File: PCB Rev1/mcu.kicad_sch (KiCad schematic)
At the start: 6 parts, among them SW3 RESET, SW4 BOOT, U7 ESP32-S3-MINI-1U-N8

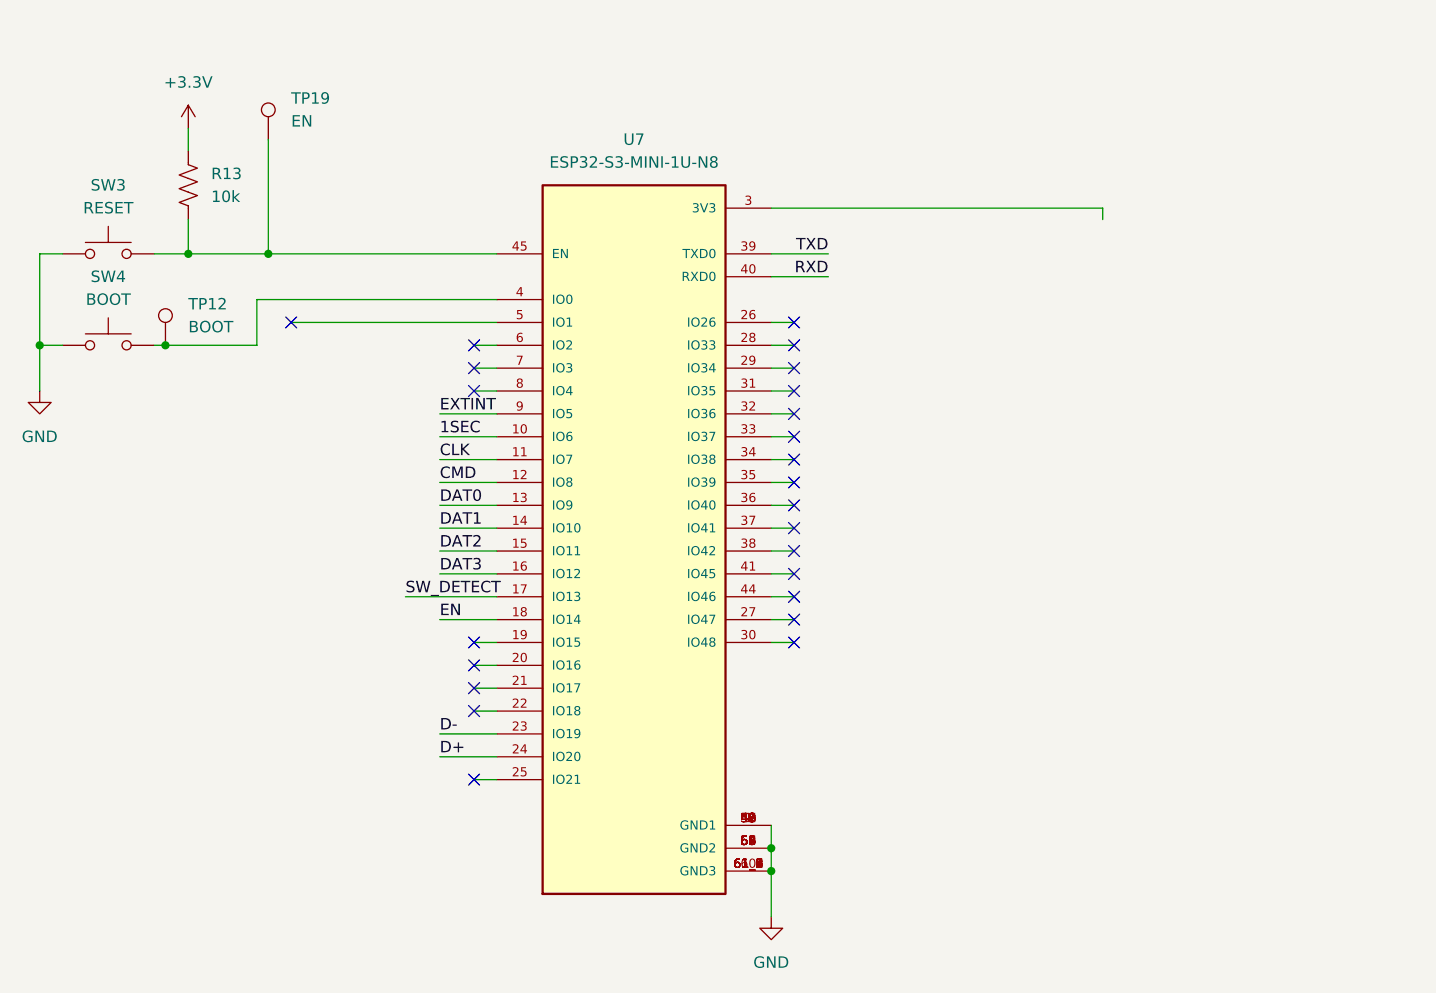
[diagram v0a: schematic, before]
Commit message: rev 2 schematic with minor changes, final send out before layout
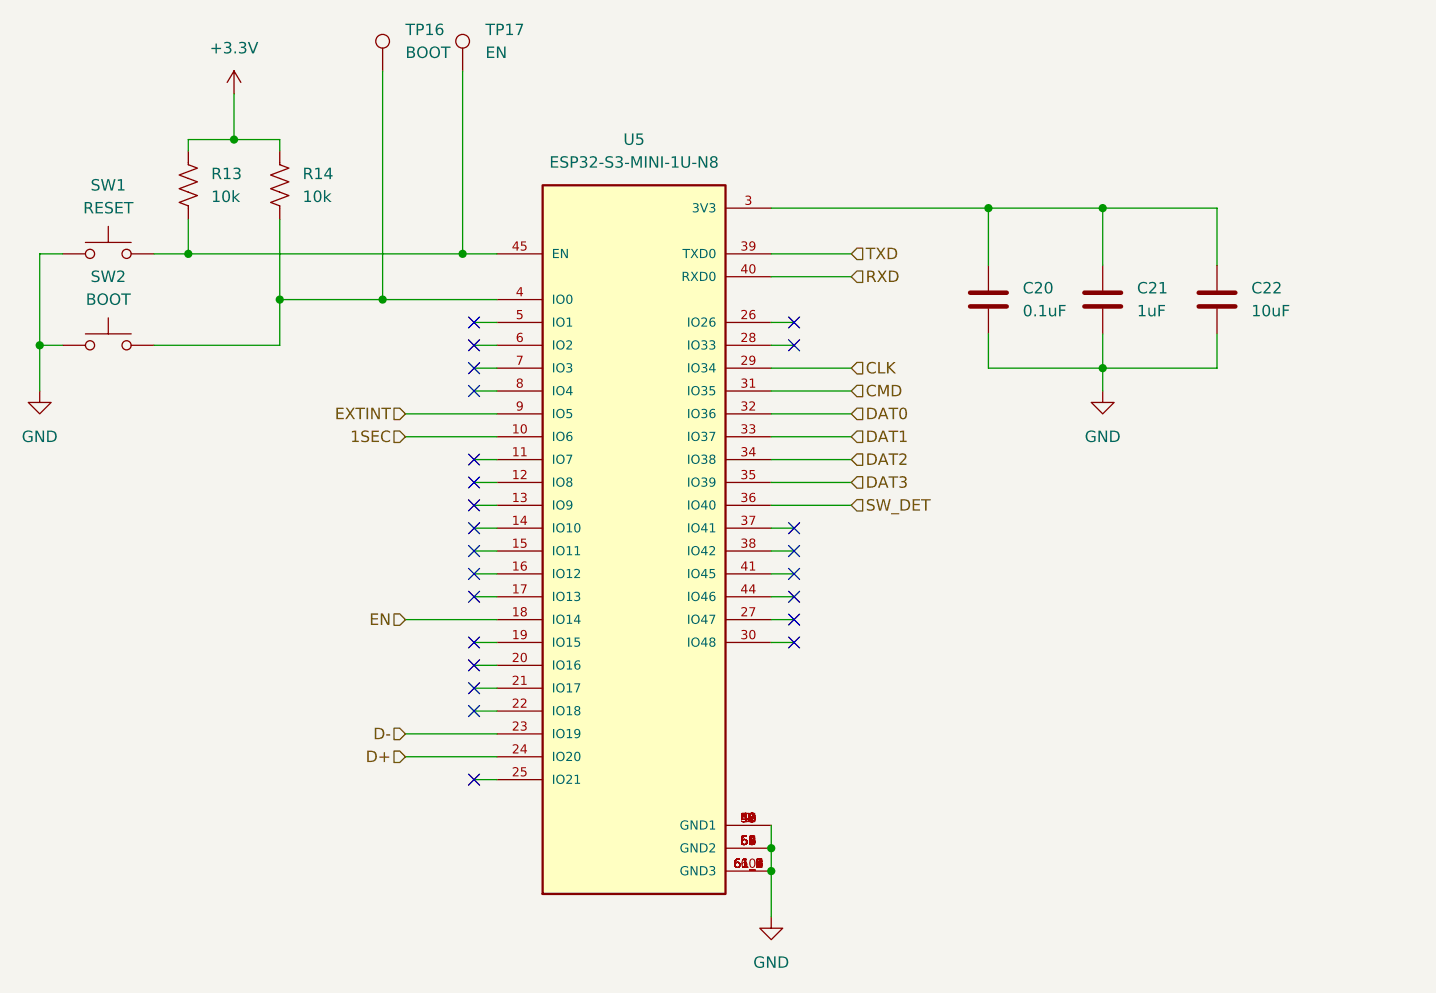
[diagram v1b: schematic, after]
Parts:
- added C20: 0.1uF, symbol Device:C
- added C21: 1uF, symbol Device:C
- added C22: 10uF, symbol Device:C
- added R14: 10k, symbol Device:R_US
- renumbered SW3 to SW1, SW4 to SW2, TP12 to TP16, TP19 to TP17, U7 to U5
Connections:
- net +3.3V: now also R14.1
- net CLK: now also U5.29 (IO34); no longer U5.11 (IO7)
- net CMD: now also U5.31 (IO35); no longer U5.12 (IO8)
- net DAT0: now also U5.32 (IO36); no longer U5.13 (IO9)
- net DAT1: now also U5.33 (IO37); no longer U5.14 (IO10)
- net DAT2: now also U5.34 (IO38); no longer U5.15 (IO11)
- net DAT3: now also U5.35 (IO39); no longer U5.16 (IO12)
- net GND: now also C20.2, C21.2, C22.2
- net at SW2.2, TP16.1, U5.4 (IO0): now also R14.2
- net at U5.3 (3V3): now also C20.1, C21.1, C22.1
- net SW_DET: now reaches U5.36 (IO40)
- net SW_DETECT: no longer names the net of U5.17 (IO13)
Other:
- moved on the sheet: TP16, TP17

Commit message: added PCB rev2!
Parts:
- removed C22: 10uF, symbol Device:C
- added C19: 0.1uF, Capacitor_SMD:C_0603_1608Metric, symbol Device:C
- C20: value 0.1uF -> 1uF; footprint (none) -> Capacitor_SMD:C_0603_1608Metric; Part # (none) -> LMK107BJ105KAHT
- C21: value 1uF -> 10uF; footprint (none) -> Capacitor_SMD:C_0805_2012Metric; Part # (none) -> GCM21BR71A106KE22K
- R13, R14: footprint (none) -> Resistor_SMD:R_0603_1608Metric; Part # (none) -> RK73H1JTTD1002F
- SW1: footprint (none) -> footprints:SW_TL1105TF160Q; Part # (none) -> TL1105SPF100Q
- SW2: footprint (none) -> footprints:SW_TL1105TF160Q; Part # (none) -> TL1105TF160Q
- TP16, TP17: footprint (none) -> footprints:TP_245X165; Part # (none) -> rct-0c
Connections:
- net +3.3V is gone; now on net 3.3V: R13.1, R14.1
- net GND: now also U5.61 (GND1), U5.66 (GND1), U5.67 (GND1), U5.68 (GND1), U5.69 (GND1), U5.70 (GND1), U5.71 (GND1), U5.72 (GND1), U5.73 (GND1), C19.2
- net 3.3V: now reaches C20.1, C21.1, U5.3 (3V3)
- net 3.3V: now also C19.1
- net IO41: now reaches U5.37 (IO41)
- net IO42: now reaches U5.38 (IO42)
- net IO45: now reaches U5.41 (IO45)
- net IO46: now reaches U5.44 (IO46)
- net IO3: now reaches U5.7 (IO3)
- net 1SEC renamed IO6
- net CLK renamed IO34
- net CMD renamed IO35
- net D+ renamed IO20
- net D- renamed IO19
- net DAT0 renamed IO36
- net DAT1 renamed IO37
- net DAT2 renamed IO38
- net DAT3 renamed IO39
- net EN: no longer names the net of U5.18 (IO14)
- net EXTINT renamed IO5
- net SW_DET renamed IO40
- no-connect marks 24 -> 20
